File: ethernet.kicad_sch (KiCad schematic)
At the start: 67 parts, among them Q6001 DMG1012T, Q6002 DMG1012T, U6001 HR911130A, U6002 RTL8211FD-CG, U6003 AM6231ASGGGAALW, X6001 ECS-2520MV-250-BN-TR

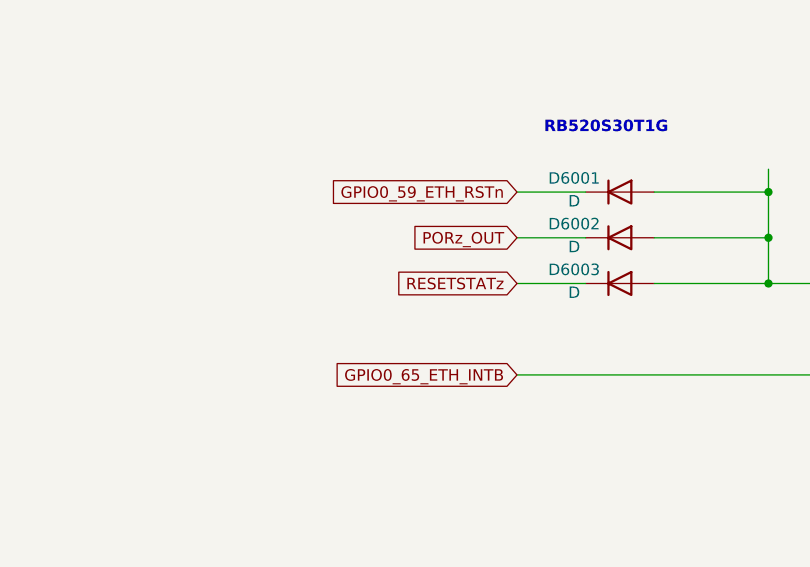
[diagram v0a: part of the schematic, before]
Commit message: Finished SoC schematic
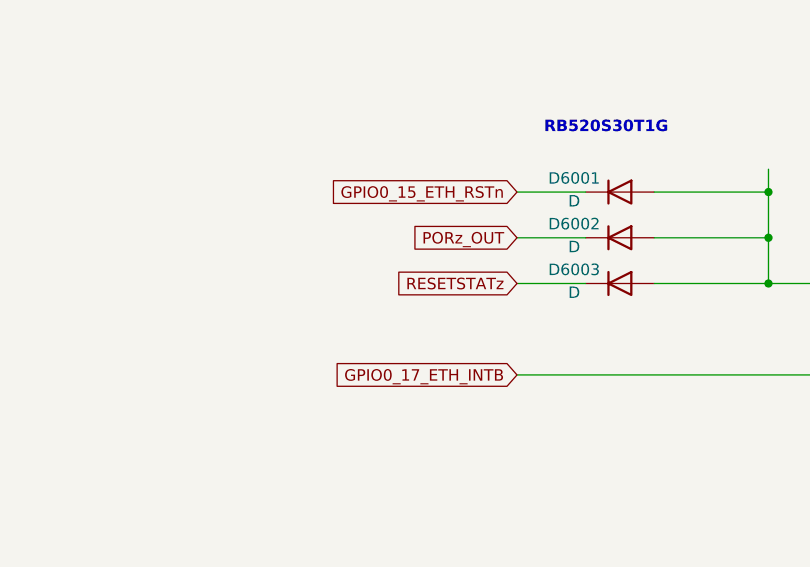
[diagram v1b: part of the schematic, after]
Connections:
- net GPIO0_59_ETH_RSTn renamed GPIO0_15_ETH_RSTn
- net GPIO0_65_ETH_INTB renamed GPIO0_17_ETH_INTB
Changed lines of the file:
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@@
 		)
 	)
-	(global_label "GPIO0_59_ETH_RSTn"
+	(global_label "GPIO0_15_ETH_RSTn"
 		(shape input)
 		(at 142.24 288.29 180)
@@
 		)
 	)
-	(global_label "GPIO0_65_ETH_INTB"
+	(global_label "GPIO0_17_ETH_INTB"
 		(shape input)
 		(at 142.24 308.61 180)

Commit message: Finished overall schematic. Fixing errors and warnings from ERC
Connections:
- net GPIO0_15_ETH_RSTn renamed ETH_RSTn
- net GPIO0_17_ETH_INTB renamed ETH_INTn
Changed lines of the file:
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@@
 	)
 	(junction
-		(at 170.18 288.29)
-		(diameter 0)
-		(color 0 0 0 0)
-	)
-	(junction
 		(at 182.88 102.87)
 		(diameter 0)
@@
 	(wire
 		(pts
-			(xy 626.11 74.93) (xy 600.71 74.93)
+			(xy 617.22 74.93) (xy 600.71 74.93)
 		)
 		(stroke
@@
 	(wire
 		(pts
-			(xy 170.18 285.75) (xy 170.18 288.29)
-		)
-		(stroke
-			(width 0)
-			(type default)
-		)
-	)
-	(wire
-		(pts
 			(xy 349.25 224.79) (xy 339.09 224.79)
 		)
@@
 		)
 	)
-	(label "ETH_MDIO"
-		(at 626.11 74.93 180)
-		(effects
-			(font
-				(size 1.27 1.27)
-				(thickness 0.254)
-				(bold yes)
-			)
-			(justify right bottom)
-		)
-	)
 	(label "ETH_RD0"
 		(at 553.72 74.93 180)
@@
 		)
 	)
-	(label "ETH_MDC"
-		(at 245.11 182.88 0)
-		(effects
-			(font
-				(size 1.27 1.27)
-				(thickness 0.254)
-				(bold yes)
-			)
-			(justify left bottom)
-		)
-	)
 	(label "ETH_PHY_RD0"
 		(at 245.11 142.24 0)
@@
 		)
 	)
-	(label "ETH_MDIO"
-		(at 245.11 185.42 0)
-		(effects
-			(font
-				(size 1.27 1.27)
-				(thickness 0.254)
-				(bold yes)
-			)
-			(justify left bottom)
-		)
-	)
 	(label "ETH_RD1"
 		(at 553.72 78.74 180)
@@
 		)
 	)
-	(global_label "GPIO0_15_ETH_RSTn"
+	(global_label "ETH_MDIO"
+		(shape input)
+		(at 617.22 74.93 0)
+		(fields_autoplaced yes)
+		(effects
+			(font
+				(size 1.27 1.27)
+				(thickness 0.1588)
+			)
+			(justify left)
+		)
+		(property "Intersheetrefs" "${INTERSHEET_REFS}"
+			(at 629.2766 74.93 0)
+			(effects
+				(font
+					(size 1.27 1.27)
+				)
+				(justify left)
+				(hide yes)
+			)
+		)
+	)
+	(global_label "ETH_MDIO"
+		(shape input)
+		(at 245.11 185.42 180)
+		(fields_autoplaced yes)
+		(effects
+			(font
+				(size 1.27 1.27)
+				(thickness 0.1588)
+			)
+			(justify right)
+		)
+		(property "Intersheetrefs" "${INTERSHEET_REFS}"
+			(at 233.0534 185.42 0)
+			(effects
+				(font
+					(size 1.27 1.27)
+				)
+				(justify right)
+				(hide yes)
+			)
+		)
+	)
+	(global_label "ETH_RSTn"
 		(shape input)
 		(at 142.24 288.29 180)
@@
 		)
 		(property "Intersheetrefs" "${INTERSHEET_REFS}"
-			(at 120.205 288.29 0)
+			(at 130.244 288.29 0)
+			(effects
+				(font
+					(size 1.27 1.27)
+				)
+				(justify right)
+				(hide yes)
+			)
+		)
+	)
+	(global_label "ETH_MDC"
+		(shape input)
+		(at 245.11 182.88 180)
+		(fields_autoplaced yes)
+		(effects
+			(font
+				(size 1.27 1.27)
+				(thickness 0.1588)
+			)
+			(justify right)
+		)
+		(property "Intersheetrefs" "${INTERSHEET_REFS}"
+			(at 233.7187 182.88 0)
 			(effects
 				(font
@@
 		)
 	)
-	(global_label "GPIO0_17_ETH_INTB"
+	(global_label "ETH_INTn"
 		(shape input)
 		(at 142.24 308.61 180)
@@
 		)
 		(property "Intersheetrefs" "${INTERSHEET_REFS}"
-			(at 120.6282 308.61 0)
+			(at 130.7882 308.61 0)
 			(effects
 				(font

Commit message: Fixed ERC errors and warnings (zero errors and zero warnings)
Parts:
- removed R6004: 1k, symbol Device:R
- added TP6001: TestPoint, symbol Connector:TestPoint
- R6005: value 1k -> 2.2k
- renumbered U6003 to U1001
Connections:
- net ETH_CLKOUT: now reaches U6002.35 (CLK_OUT)
- net ETH_CLKOUT: now also TP6001.1
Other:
- moved on the sheet: R6005

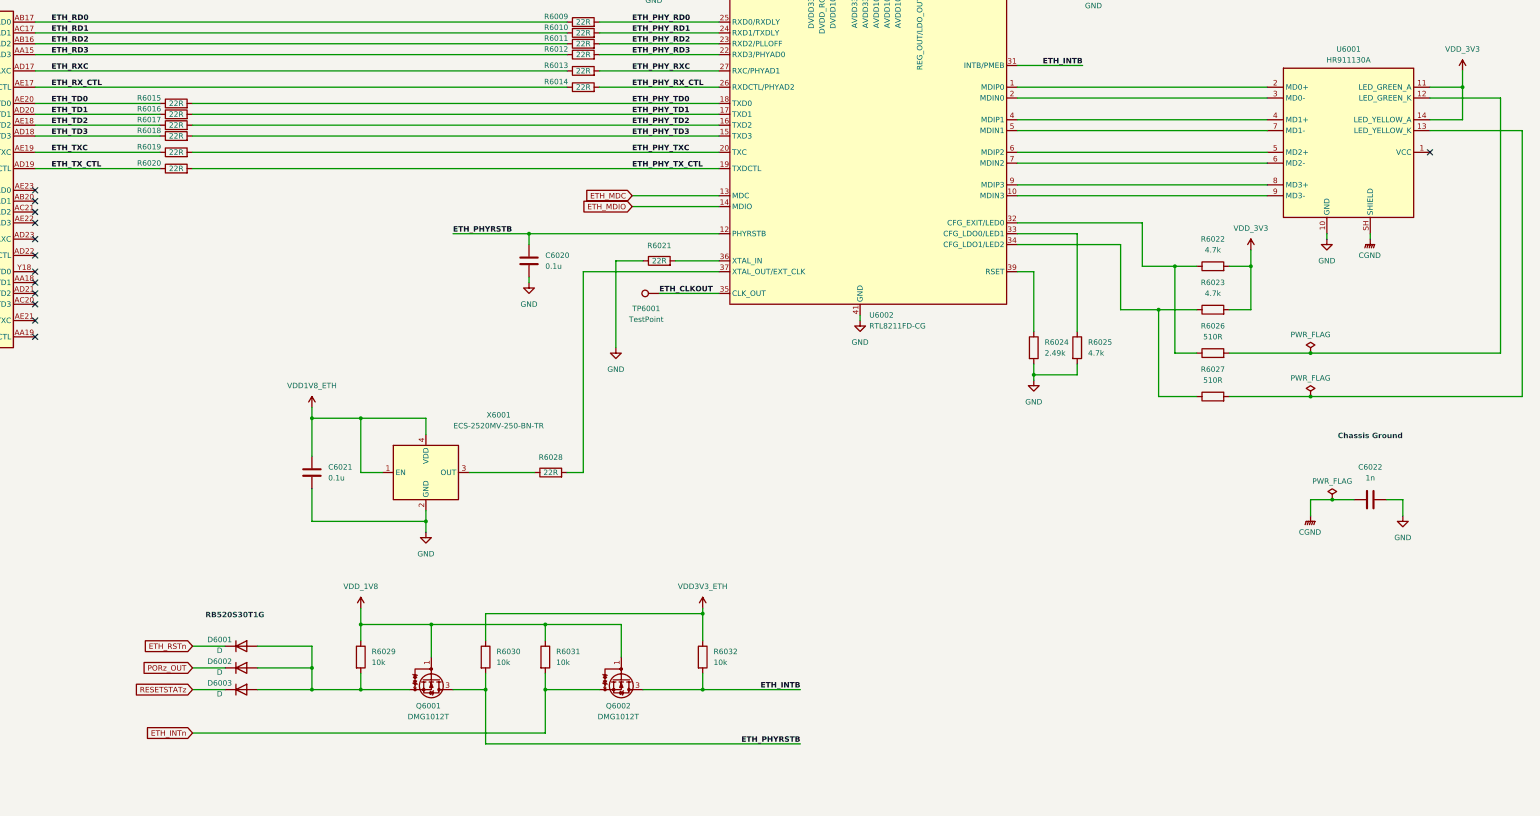
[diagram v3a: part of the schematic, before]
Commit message: Labeled all nets and added some footprints
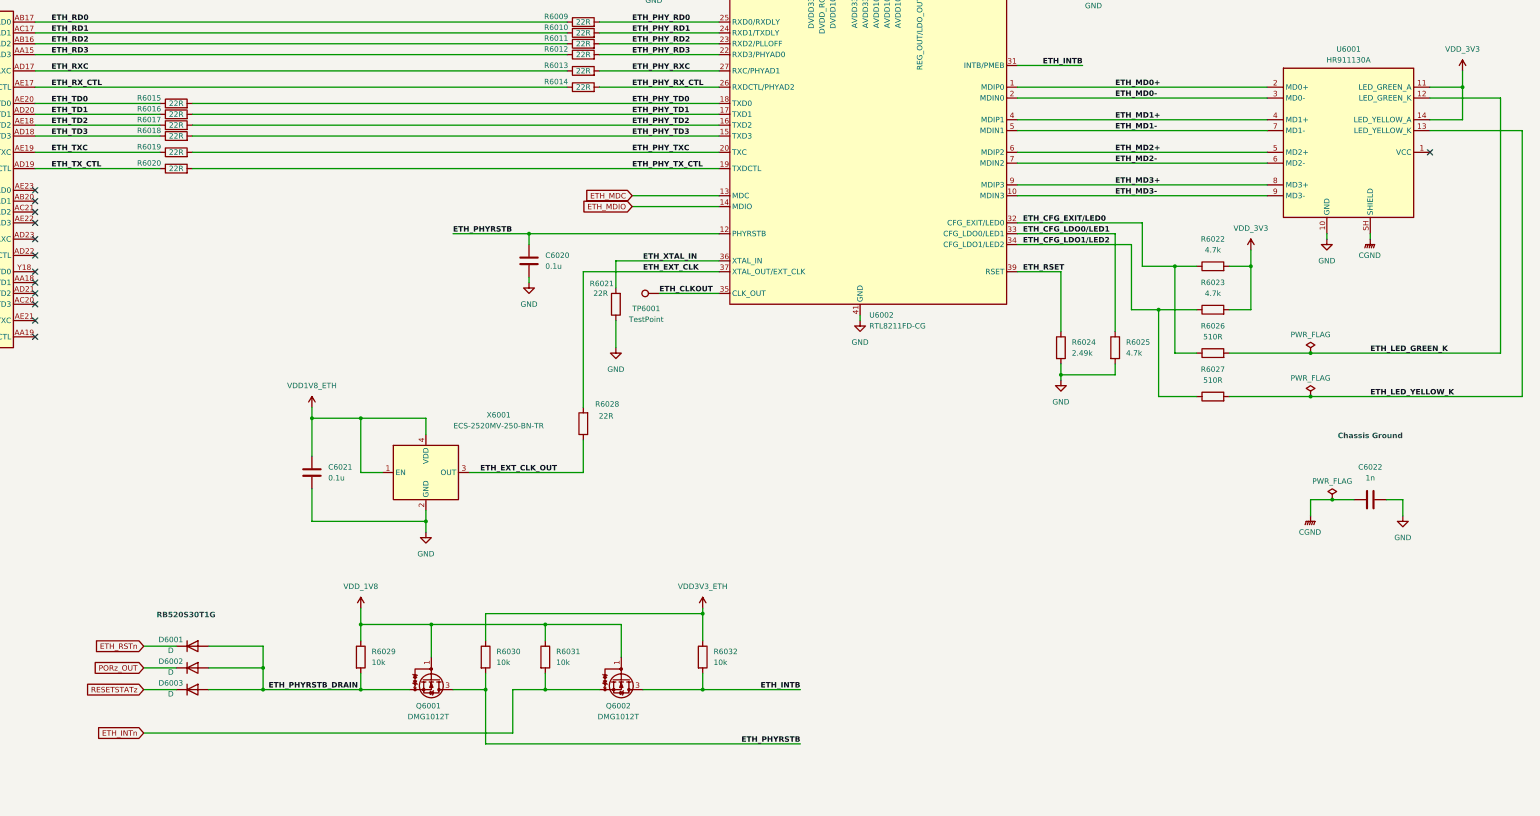
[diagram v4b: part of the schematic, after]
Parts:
- U1001: footprint (none) -> AM6231ASGGGAALW:BGA425C50P25X25_1300X1300X89
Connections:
- net ETH_PHYRSTB_DRAIN: now reaches D6001.2 (A), D6002.2 (A), D6003.2 (A), Q6001.2 (S), R6029.2
- net ETH_CFG_EXIT/LED0: now reaches R6022.1, R6026.1, U6002.32 (CFG_EXIT/LED0)
- net ETH_LED_GREEN_K: now reaches R6026.2, U6001.12 (LED_GREEN_K)
- net ETH_CFG_LDO1/LED2: now reaches R6023.1, R6027.1, U6002.34 (CFG_LDO1/LED2)
- net ETH_RSET: now reaches R6024.1, U6002.39 (RSET)
- net ETH_CFG_LDO0/LED1: now reaches R6025.1, U6002.33 (CFG_LDO0/LED1)
- net ETH_LED_YELLOW_K: now reaches R6027.2, U6001.13 (LED_YELLOW_K)
- net ETH_EXT_CLK_OUT: now reaches R6028.1, X6001.3 (OUT)
- net ETH_EXT_CLK: now reaches R6028.2, U6002.37 (XTAL_OUT/EXT_CLK)
- net ETH_MD0+: now reaches U6001.2 (MD0+), U6002.1 (MDIP0)
- net ETH_MD3-: now reaches U6001.9 (MD3-), U6002.10 (MDIN3)
- net ETH_MD0-: now reaches U6001.3 (MD0-), U6002.2 (MDIN0)
- net ETH_XTAL_IN: now reaches R6021.2, U6002.36 (XTAL_IN)
- net ETH_MD1+: now reaches U6001.4 (MD1+), U6002.4 (MDIP1)
- net ETH_MD1-: now reaches U6001.7 (MD1-), U6002.5 (MDIN1)
- net ETH_MD2+: now reaches U6001.5 (MD2+), U6002.6 (MDIP2)
- net ETH_MD2-: now reaches U6001.6 (MD2-), U6002.7 (MDIN2)
- net ETH_MD3+: now reaches U6001.8 (MD3+), U6002.9 (MDIP3)
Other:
- moved on the sheet: D6001, D6002, D6003, R6021, R6024, R6025, R6028

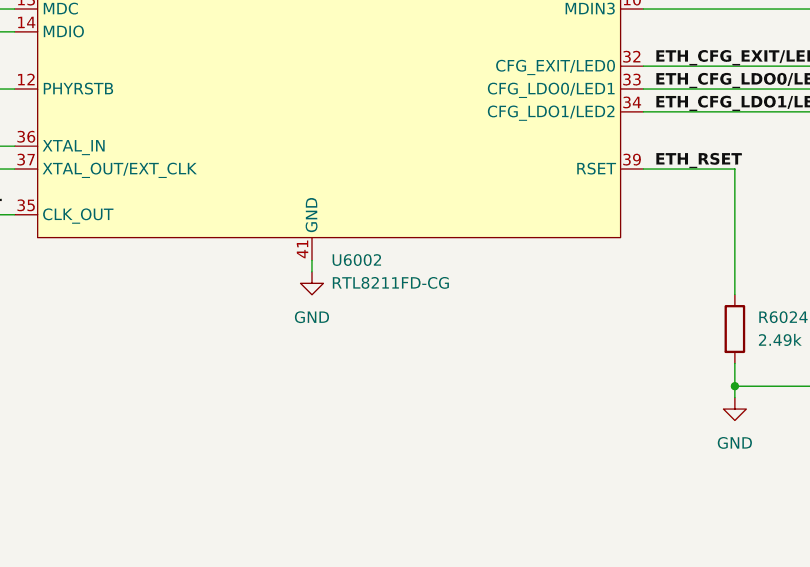
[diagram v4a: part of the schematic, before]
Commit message: Added some footprints for important ICs
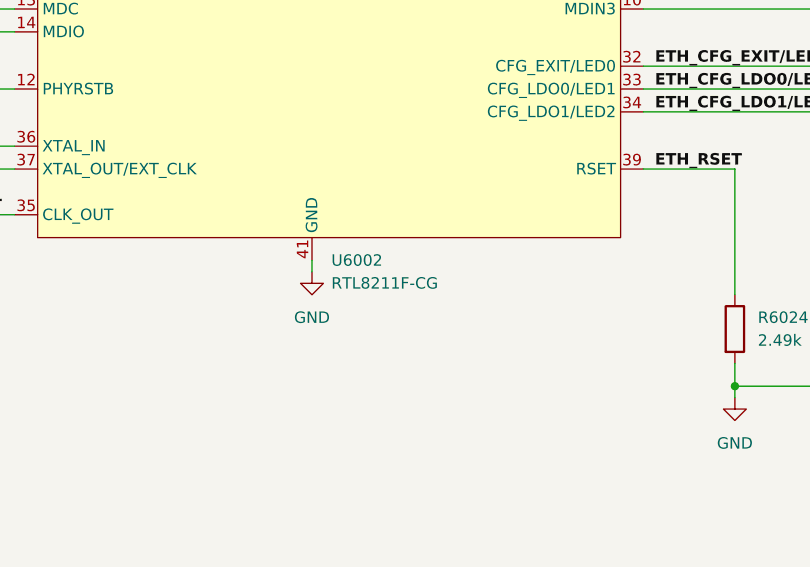
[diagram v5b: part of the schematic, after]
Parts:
- removed U6002: RTL8211FD-CG, symbol SoftServicesSymbolLibrary:RTL8211FD-CG
- added U6002: RTL8211F-CG, Package_DFN_QFN:QFN-40-1EP_5x5mm_P0.4mm_EP3.6x3.6mm, symbol SoftServicesSymbolLibrary:RTL8211F-CG
- U6001: footprint (none) -> HR911130A:HR911130A
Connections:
- net ETH_CFG_EXIT/LED0: now also U6002.32 (CFG_EXIT/LED0)
- net ETH_CFG_LDO0/LED1: now also U6002.33 (CFG_LDO0/LED1)
- net ETH_CFG_LDO1/LED2: now also U6002.34 (CFG_LDO1/LED2)
- net ETH_CLKOUT: now also U6002.35 (CLK_OUT)
- net ETH_EXT_CLK: now also U6002.37 (XTAL_OUT/EXT_CLK)
- net ETH_INTB: now also U6002.31 (INTB/PMEB)
- net ETH_MD0+: now also U6002.1 (MDIP0)
- net ETH_MD0-: now also U6002.2 (MDIN0)
- net ETH_MD1+: now also U6002.4 (MDIP1)
- net ETH_MD1-: now also U6002.5 (MDIN1)
- net ETH_MD2+: now also U6002.6 (MDIP2)
- net ETH_MD2-: now also U6002.7 (MDIN2)
- net ETH_MD3+: now also U6002.9 (MDIP3)
- net ETH_MD3-: now also U6002.10 (MDIN3)
- net ETH_MDC: now also U6002.13 (MDC)
- net ETH_MDIO: now also U6002.14 (MDIO)
- net ETH_PHYRSTB: now also U6002.12 (PHYRSTB)
- net ETH_PHY_RD0: now also U6002.25 (RXD0/RXDLY)
- net ETH_PHY_RD1: now also U6002.24 (RXD1/TXDLY)
- net ETH_PHY_RD2: now also U6002.23 (RXD2/PLLOFF)
- net ETH_PHY_RD3: now also U6002.22 (RXD3/PHYAD0)
- net ETH_PHY_RXC: now also U6002.27 (RXC/PHYAD1)
- net ETH_PHY_RX_CTL: now also U6002.26 (RXDCTL/PHYAD2)
- net ETH_PHY_TD0: now also U6002.18 (TXD0)
- net ETH_PHY_TD1: now also U6002.17 (TXD1)
- net ETH_PHY_TD2: now also U6002.16 (TXD2)
- net ETH_PHY_TD3: now also U6002.15 (TXD3)
- net ETH_PHY_TXC: now also U6002.20 (TXC)
- net ETH_PHY_TX_CTL: now also U6002.19 (TXDCTL)
- net ETH_RSET: now also U6002.39 (RSET)
- net ETH_XTAL_IN: now also U6002.36 (XTAL_IN)
- net GND: now also U6002.41 (GND)
- net VDD1V0_ETH: now also U6002.21 (DVDD10), U6002.3 (AVDD10), U6002.38 (AVDD10), U6002.8 (AVDD10)
- net VDD1V8_ETH: now also U6002.28 (DVDD_RG)
- net VDD3V3_ETH: now also U6002.29 (DVDD33)
- net at C6001.1, C6002.1, C6003.1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: now also U6002.11 (AVDD33), U6002.40 (AVDD33)
- net at L6001.1: now also U6002.30 (REG_OUT/LDO_OUT)
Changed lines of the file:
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@@
+	)
+	(symbol
+		(lib_id "SoftServicesSymbolLibrary:RTL8211F-CG")
+		(at 295.91 176.53 0)
+		(unit 1)
+		(exclude_from_sim no)
+		(in_bom yes)
+		(on_board yes)
+		(dnp no)
+		(fields_autoplaced yes)
+		(property "Reference" "U6002"
+			(at 300.5933 210.82 0)
+			(effects
+				(font
+					(size 1.27 1.27)
+				)
+				(justify left)
+			)
+		)
+		(property "Value" "RTL8211F-CG"
+			(at 300.5933 213.36 0)
+			(effects
+				(font
+					(size 1.27 1.27)
+				)
+				(justify left)
+			)
+		)
+		(property "Footprint" "Package_DFN_QFN:QFN-40-1EP_5x5mm_P0.4mm_EP3.6x3.6mm"
+			(at 295.91 176.53 0)
+			(effects
+				(font
+					(size 1.27 1.27)
+				)
+				(hide yes)
+			)
+		)
+		(property "Datasheet" ""
+			(at 295.91 176.53 0)
+			(effects
+				(font
+					(size 1.27 1.27)
+				)
+				(hide yes)
+			)
+		)
+		(property "Description" ""
+			(at 295.91 176.53 0)
+			(effects
+				(font
+					(size 1.27 1.27)
+				)
+				(hide yes)
+			)
+		)
+		(pin "1"
+		)
+		(pin "19"
+		)
+		(pin "26"
+		)
+		(pin "13"
+		)
+		(pin "36"
+		)
+		(pin "33"
+		)
+		(pin "11"
+		)
+		(pin "12"
+		)
+		(pin "39"
+		)
+		(pin "34"
+		)
+		(pin "23"
+		)
+		(pin "18"
+		)
+		(pin "24"
+		)
+		(pin "17"
+		)
+		(pin "27"
+		)
+		(pin "22"
+		)
+		(pin "14"
+		)
+		(pin "5"
+		)
+		(pin "31"
+		)
+		(pin "25"
+		)
+		(pin "21"
+		)
+		(pin "3"
+		)
+		(pin "2"
+		)
+		(pin "15"
+		)
+		(pin "16"
+		)
+		(pin "28"
+		)
+		(pin "6"
+		)
+		(pin "35"
+		)
+		(pin "41"
+		)
+		(pin "7"
+		)
+		(pin "37"
+		)
+		(pin "29"
+		)
+		(pin "20"
+		)
+		(pin "9"
+		)
+		(pin "32"
+		)
+		(pin "38"
+		)
+		(pin "40"
+		)
+		(pin "10"
+		)
+		(pin "4"
+		)
+		(pin "30"
+		)
+		(pin "8"
+		)
+		(instances
+			(project ""
+				(path "/b43b7bca-e50d-42ec-8ff0-e0016dfefe0a/6c7f2037-3077-4980-ab71-7ff032fdfd6e"
+					(reference "U6002")
+					(unit 1)
+				)
+			)
+		)
 	)
 	(symbol
@@
 	)
 	(symbol
-		(lib_id "SoftServicesSymbolLibrary:RTL8211FD-CG")
-		(at 295.91 176.53 0)
-		(unit 1)
-		(exclude_from_sim no)
-		(in_bom yes)
-		(on_board yes)
-		(dnp no)
-		(fields_autoplaced yes)
-		(property "Reference" "U6002"
-			(at 300.5933 210.82 0)
-			(effects
-				(font
-					(size 1.27 1.27)
-				)
-				(justify left)
-			)
-		)
-		(property "Value" "RTL8211FD-CG"
-			(at 300.5933 213.36 0)
-			(effects
-				(font
-					(size 1.27 1.27)
-				)
-				(justify left)
-			)
-		)
-		(property "Footprint" ""
-			(at 295.91 176.53 0)
-			(effects
-				(font
-					(size 1.27 1.27)
-				)
-				(hide yes)
-			)
-		)
-		(property "Datasheet" ""
-			(at 295.91 176.53 0)
-			(effects
-				(font
-					(size 1.27 1.27)
-				)
-				(hide yes)
-			)
-		)
-		(property "Description" ""
-			(at 295.91 176.53 0)
-			(effects
-				(font
-					(size 1.27 1.27)
-				)
-				(hide yes)
-			)
-		)
-		(pin "22"
-		)
-		(pin "25"
-		)
-		(pin "8"
-		)
-		(pin "28"
-		)
-		(pin "13"
-		)
-		(pin "26"
-		)
-		(pin "38"
-		)
-		(pin "14"
-		)
-		(pin "40"
-		)
-		(pin "19"
-		)
-		(pin "24"
-		)
-		(pin "23"
-		)
-		(pin "16"
-		)
-		(pin "20"
-		)
-		(pin "29"
-		)
-		(pin "21"
-		)
-		(pin "4"
-		)
-		(pin "5"
-		)
-		(pin "6"
-		)
-		(pin "7"
-		)
-		(pin "9"
-		)
-		(pin "10"
-		)
-		(pin "32"
-		)
-		(pin "33"
-		)
-		(pin "34"
-		)
-		(pin "39"
-		)
-		(pin "12"
-		)
-		(pin "31"
-		)
-		(pin "37"
-		)
-		(pin "35"
-		)
-		(pin "18"
-		)
-		(pin "30"
-		)
-		(pin "41"
-		)
-		(pin "36"
-		)
-		(pin "15"
-		)
-		(pin "3"
-		)
-		(pin "1"
-		)
-		(pin "17"
-		)
-		(pin "11"
-		)
-		(pin "27"
-		)
-		(pin "2"
-		)
-		(instances
-			(project ""
-				(path "/b43b7bca-e50d-42ec-8ff0-e0016dfefe0a/6c7f2037-3077-4980-ab71-7ff032fdfd6e"
-					(reference "U6002")
-					(unit 1)
-				)
-			)
-		)
-	)
-	(symbol
 		(lib_id "power:GND")
 		(at 196.85 261.62 0)
@@
 			)
 		)
-		(property "Footprint" ""
+		(property "Footprint" "HR911130A:HR911130A"
 			(at 412.75 171.45 0)
 			(effects

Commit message: Added more IC footprints
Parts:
- X6001: footprint (none) -> ECS-2520MV-250-BN-TR:ECS2520MV250BNTR
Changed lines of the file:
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@@
 			)
 		)
-		(property "Footprint" ""
+		(property "Footprint" "ECS-2520MV-250-BN-TR:ECS2520MV250BNTR"
 			(at 196.85 247.65 0)
 			(effects

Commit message: Added almost all passive component footprints
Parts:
- D6001, D6002, D6003: footprint (none) -> Diode_SMD:D_SOD-523
- FB6001, FB6002, FB6003: footprint (none) -> Resistor_SMD:R_0402_1005Metric
- TP6001: footprint (none) -> TestPoint:TestPoint_Pad_1.0x1.0mm
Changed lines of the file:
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@@
 			)
 		)
-		(property "Footprint" ""
+		(property "Footprint" "Diode_SMD:D_SOD-523"
 			(at 142.24 298.45 0)
 			(effects
@@
 			)
 		)
-		(property "Footprint" ""
+		(property "Footprint" "Resistor_SMD:R_0402_1005Metric"
 			(at 208.28 91.948 90)
 			(effects
@@
 			)
 		)
-		(property "Footprint" ""
+		(property "Footprint" "TestPoint:TestPoint_Pad_1.0x1.0mm"
 			(at 251.46 200.66 0)
 			(effects
@@
 			)
 		)
-		(property "Footprint" ""
+		(property "Footprint" "Diode_SMD:D_SOD-523"
 			(at 142.24 288.29 0)
 			(effects
@@
 			)
 		)
-		(property "Footprint" ""
+		(property "Footprint" "Resistor_SMD:R_0402_1005Metric"
 			(at 236.22 118.618 90)
 			(effects
@@
 			)
 		)
-		(property "Footprint" ""
+		(property "Footprint" "Diode_SMD:D_SOD-523"
 			(at 142.24 293.37 0)
 			(effects
@@
 			)
 		)
-		(property "Footprint" ""
+		(property "Footprint" "Resistor_SMD:R_0402_1005Metric"
 			(at 381 56.388 90)
 			(effects
